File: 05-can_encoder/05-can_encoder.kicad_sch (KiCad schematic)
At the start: 14 parts, among them IC1 STM32F072CBT6, IC2 AS5047P-ATSM, U1 SN65HVD230DR, U2 LM3940IMPX-3.3_NOPB

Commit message: layout draft
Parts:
- added C11, C12: 100nF, Capacitor_SMD:C_0603_1608Metric, symbol Device:C
- added C13: 1uF, Capacitor_SMD:C_0603_1608Metric, symbol Device:C
- added H1, H2, H3, H4: MountingHole_Pad, MountingHole:MountingHole_2.2mm_M2_DIN965_Pad, symbol Mechanical:MountingHole_Pad
- added J1: Conn_02x05_Odd_Even, Connector_PinHeader_2.54mm:PinHeader_2x05_P2.54mm_Vertical, symbol Connector_Generic:Conn_02x05_Odd_Even
- added R1: 10k, Resistor_SMD:R_0603_1608Metric, symbol Device:R
- C1, C10, C2, C3, C4, C5, C6, C7, C8, C9: footprint (none) -> Capacitor_SMD:C_0603_1608Metric
- IC1: footprint QFP50P900X900X160-48N -> can_encoder:STM32F072CBT6
- IC2: footprint SOP65P640X120-14N -> can_encoder:AS5047P-ATSM
- U1: footprint D8 -> can_encoder:SN65HVD230DR
- U2: footprint LM3940IMPX-3.3_NOPB:SOT230P700X180-4N -> can_encoder:LM3940IMPX
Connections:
- net 3v3: now also C11.1, J1.9 (Pin_9)
- net 5v: now also C12.1, J1.8 (Pin_8)
- net CAN_H: now also J1.4 (Pin_4), J1.6 (Pin_6)
- net CAN_L: now also J1.3 (Pin_3), J1.5 (Pin_5)
- net GND: now also C11.2, C12.2, C13.2, H1.1, H2.1, H3.1, H4.1, J1.7 (Pin_7), R1.2
- net can_rx: now also IC1.45 (PB8); no longer IC1.32 (PA11)
- net can_tx: now also IC1.46 (PB9); no longer IC1.33 (PA12)
- net BOOT0: now reaches IC1.44 (BOOT0)
- net BOOT0: now also J1.10 (Pin_10), R1.1
- net at IC2.12 (VDD3V): now also C13.1
- new net USB_DM: IC1.32 (PA11), J1.1 (Pin_1)
- new net USB_DP: IC1.33 (PA12), J1.2 (Pin_2)
- no-connect marks 42 -> 38
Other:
- moved on the sheet: C7, C8

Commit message: wip layout diff pair
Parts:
- added R2: 120, Resistor_SMD:R_0603_1608Metric, symbol Device:R
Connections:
- net CAN_H renamed CAN+
- net CAN+: now also J1.3 (Pin_3), R2.1; no longer J1.6 (Pin_6)
- net CAN_L renamed CAN-
- net CAN-: now also J1.6 (Pin_6), R2.2; no longer J1.3 (Pin_3)
- net USB_DM renamed USB_D-
- net USB_DP renamed USB_D+

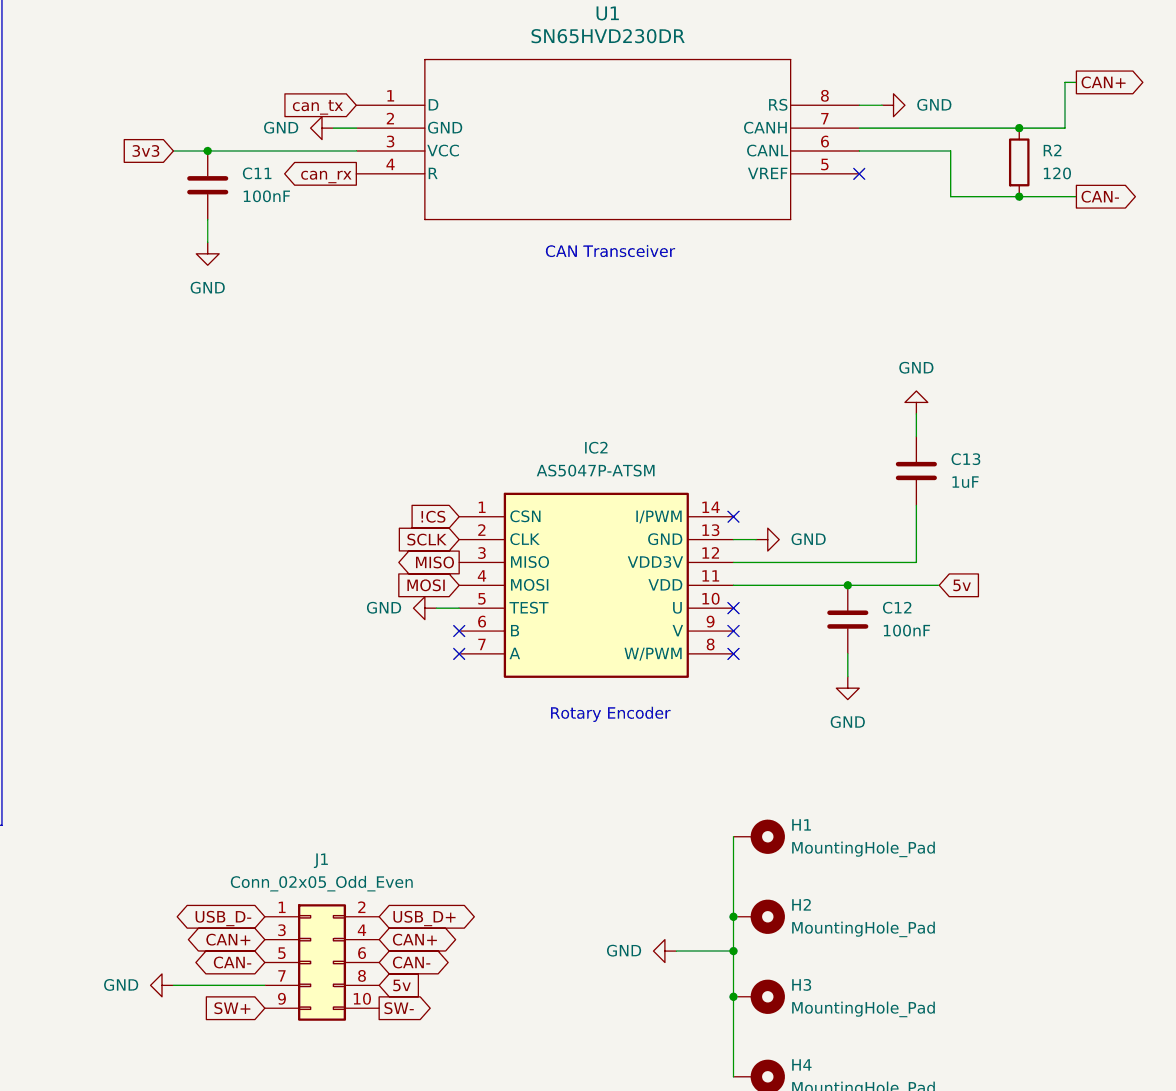
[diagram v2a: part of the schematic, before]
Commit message: layout fixes
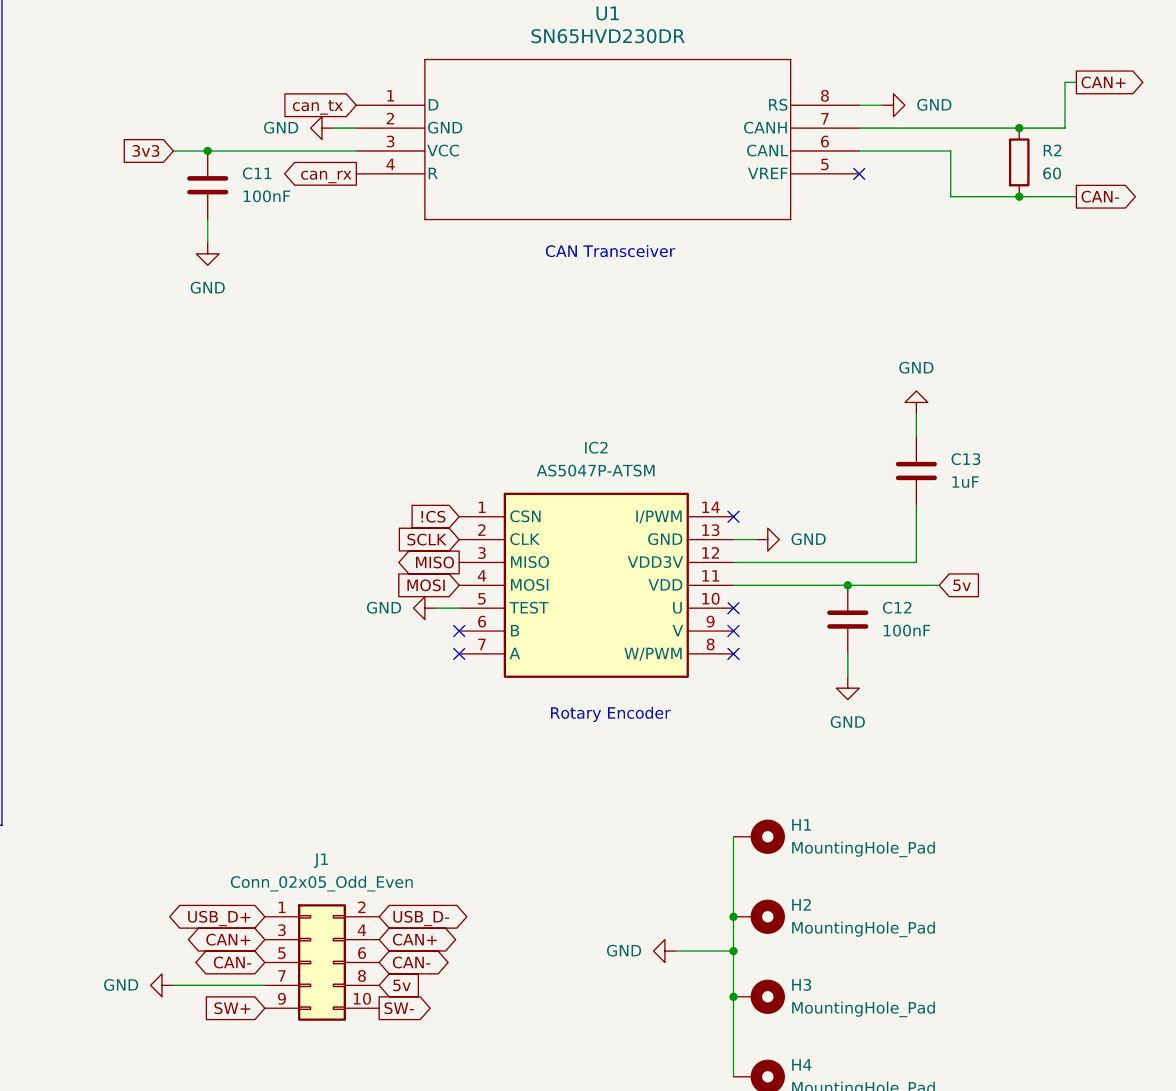
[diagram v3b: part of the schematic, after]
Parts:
- R2: value 120 -> 60
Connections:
- net USB_D+: now also J1.1 (Pin_1); no longer J1.2 (Pin_2)
- net USB_D-: now also J1.2 (Pin_2); no longer J1.1 (Pin_1)
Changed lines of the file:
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@@
+		)
+	)
+	(global_label "USB_D+"
+		(shape bidirectional)
+		(at 180.34 137.16 180)
+		(fields_autoplaced yes)
+		(effects
+			(font
+				(size 1.27 1.27)
+			)
+			(justify right)
+		)
+		(property "Intersheetrefs" "${INTERSHEET_REFS}"
+			(at 168.6235 137.16 0)
+			(effects
+				(font
+					(size 1.27 1.27)
+				)
+				(justify right)
+				(hide yes)
+			)
 		)
 	)
@@
 		)
 	)
+	(global_label "USB_D-"
+		(shape bidirectional)
+		(at 193.04 137.16 0)
+		(fields_autoplaced yes)
+		(effects
+			(font
+				(size 1.27 1.27)
+			)
+			(justify left)
+		)
+		(property "Intersheetrefs" "${INTERSHEET_REFS}"
+			(at 204.7565 137.16 0)
+			(effects
+				(font
+					(size 1.27 1.27)
+				)
+				(justify left)
+				(hide yes)
+			)
+		)
+	)
 	(global_label "3v3"
 		(shape input)
@@
 		)
 	)
-	(global_label "USB_D-"
-		(shape bidirectional)
-		(at 180.34 137.16 180)
-		(fields_autoplaced yes)
-		(effects
-			(font
-				(size 1.27 1.27)
-			)
-			(justify right)
-		)
-		(property "Intersheetrefs" "${INTERSHEET_REFS}"
-			(at 168.6235 137.16 0)
-			(effects
-				(font
-					(size 1.27 1.27)
-				)
-				(justify right)
-				(hide yes)
-			)
-		)
-	)
 	(global_label "BOOT0"
 		(shape input)
@@
 				)
 				(justify right)
-				(hide yes)
-			)
-		)
-	)
-	(global_label "USB_D+"
-		(shape bidirectional)
-		(at 193.04 137.16 0)
-		(fields_autoplaced yes)
-		(effects
-			(font
-				(size 1.27 1.27)
-			)
-			(justify left)
-		)
-		(property "Intersheetrefs" "${INTERSHEET_REFS}"
-			(at 204.7565 137.16 0)
-			(effects
-				(font
-					(size 1.27 1.27)
-				)
-				(justify left)
 				(hide yes)
 			)
@@
 			)
 		)
-		(property "Value" "120"
+		(property "Value" "60"
 			(at 266.7 54.6099 0)
 			(effects
